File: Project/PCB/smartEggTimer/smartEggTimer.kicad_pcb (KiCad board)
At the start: 2 copper layers, 72 x 72 mm, 65 parts, among them J1 Conn_01x05_Pin, J2 Conn_01x03_Pin, J3 Conn_01x03_Pin, J4 Conn_01x06_Pin, J5 Conn_01x02_Socket, J6 Conn_01x02_Socket, J7 Conn_01x03_Pin, J8 Conn_01x03_Pin, Q2 STP60NF06L, SW1 SW_Push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

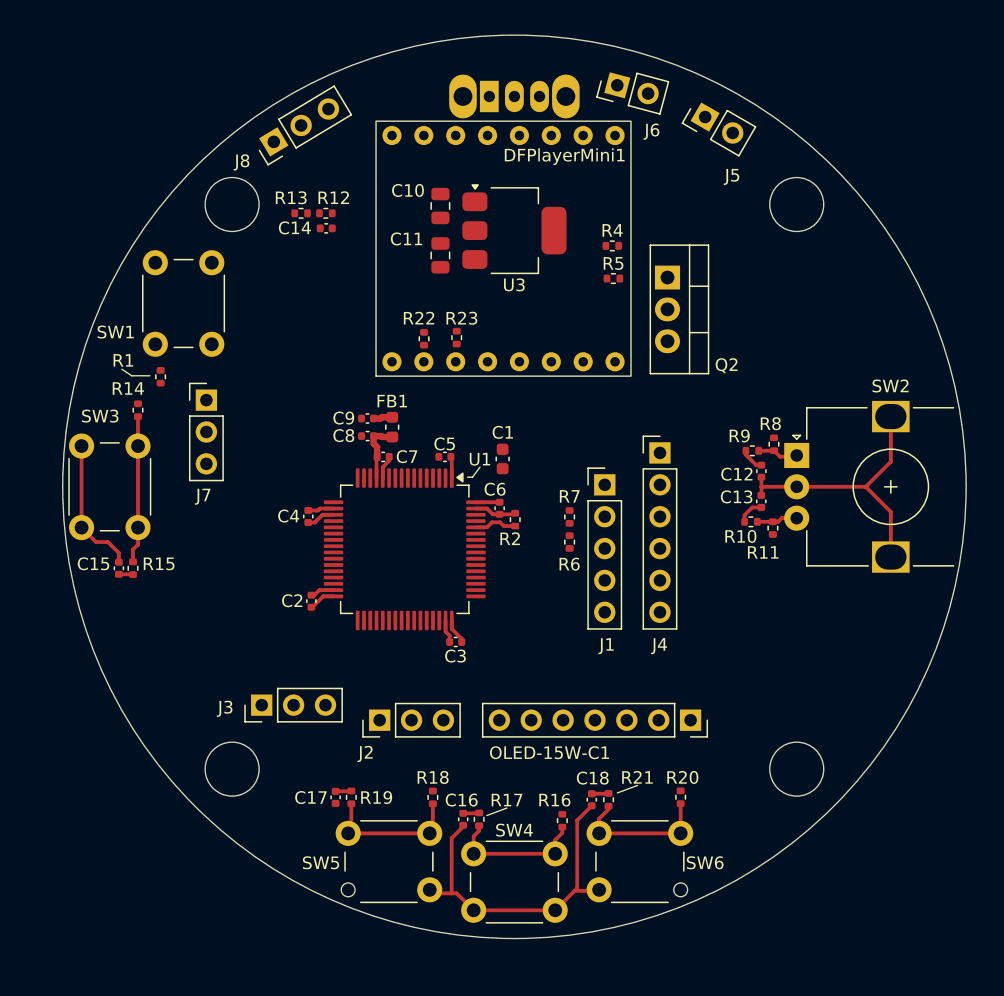
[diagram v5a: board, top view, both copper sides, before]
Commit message: finish PCB routing Further changes: - Change schematic symbol of MOSFET s.t. pin assignment is correct - Add STEP file for DFPlayer Mini - Save edited footprints to custom-parts project library - Set "exclude from BOM" attribute for components which will be soldered manually
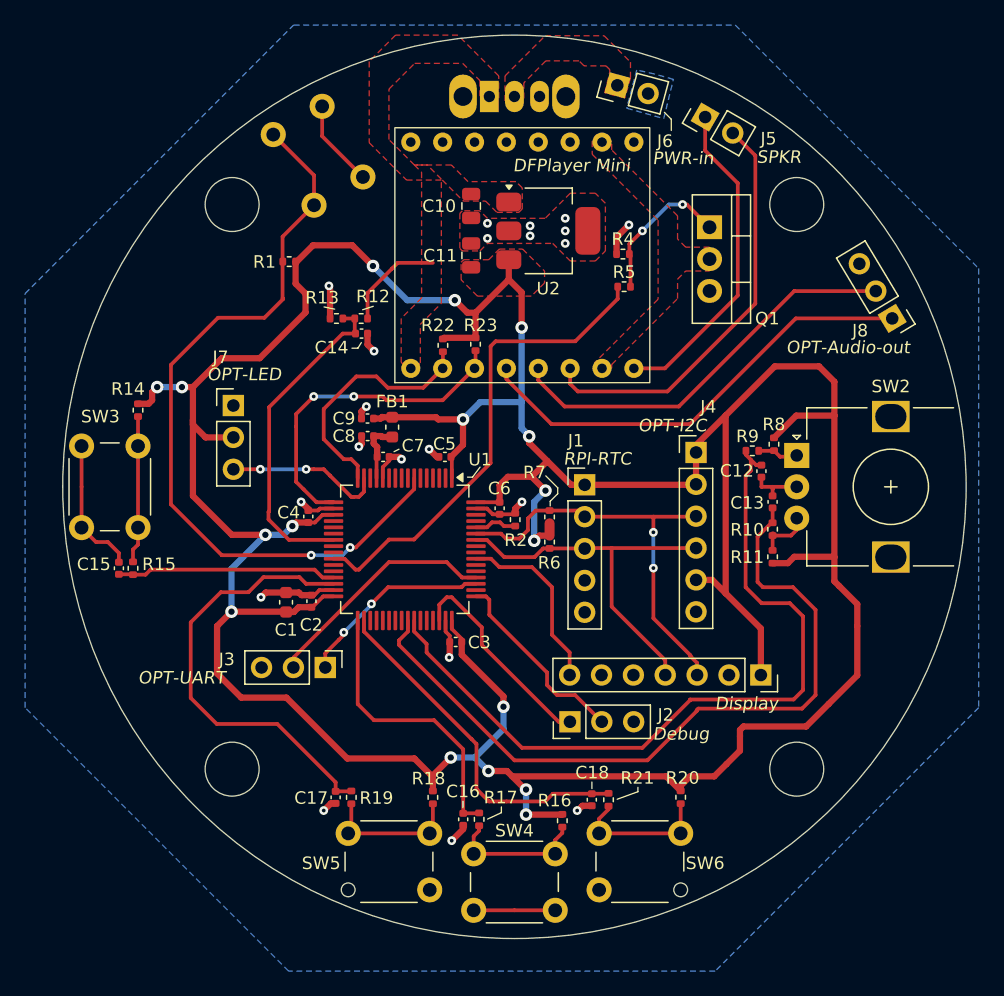
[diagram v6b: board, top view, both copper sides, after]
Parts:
- removed Q2: STP60NF06L, Package_TO_SOT_THT:TO-220-3_Vertical
- removed U3: AP7361C-33E, Package_TO_SOT_SMD:SOT-223-3_TabPin2
- added Q1: STP60NF06L, Package_TO_SOT_THT:TO-220-3_Vertical, F.Cu at (115.5, 79.3)
- added U2: AP7361C-33E, Package_TO_SOT_SMD:SOT-223-3_TabPin2, F.Cu at (102.7, 79.6)
- H1, H2: footprint MountingHole:MountingHole_4.3mm_M4 -> custom-parts:MountingHole_4.3mm_M4_Without-Screws
- H3, H8: footprint MountingHole:MountingHole_4.3mm_M4_DIN965 -> custom-parts:MountingHole_4.3mm_M4_Without-Screws
- SW1: moved to B.Cu
- SW2: footprint Rotary_Encoder:RotaryEncoder_Alps_EC12E_Vertical_H20mm -> custom-parts:RotaryEncoder_Alps_EC12E_Vertical_H20mm_Mounting-Holes-GND
- SW5: footprint Button_Switch_THT:SW_PUSH_6mm_H13mm -> custom-parts:SW_PUSH_6mm_H13mm_No-Pad_Top-Right
- SW6: footprint Button_Switch_THT:SW_PUSH_6mm_H13mm -> custom-parts:SW_PUSH_6mm_H13mm_No-Pad_Top-Left
- SW7: footprint Button_Switch_THT:SW_Slide_SPDT_Angled_CK_OS102011MA1Q -> custom-parts:SW_Slide_SPDT_Angled_CK_OS102011MA1Q_Protruding
- moved J8 51.3 mm to (130.1, 86.6), turned to -149 degrees
- moved SW1 21.3 mm to (87.9, 75.3), turned to 120 degrees
- moved C1 20.7 mm to (81.8, 109.2)
- moved J2 15.2 mm to (104.4, 118.7)
- moved R1 13.8 mm to (82.0, 82.0), turned to 0 degrees
- moved C14 8.84 mm to (87.8, 87.8)
- moved R12 8.84 mm to (87.8, 86.6)
- moved R13 8.84 mm to (85.8, 86.6)
- moved OLED-15W-C1 6.66 mm to (119.6, 115.0)
- moved J3 5.89 mm to (84.9, 114.4), turned to -90 degrees
- moved J4 2.88 mm to (114.5, 97.3)
- moved C10 2.45 mm to (96.5, 77.6)
- moved C11 2.45 mm to (96.5, 81.6)
- moved R11 2.29 mm to (120.6, 105.6)
- moved J7 2.19 mm to (77.6, 93.5)
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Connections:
- net Net-(Q2-D) renamed /DFPlayer-Minus
- J5 pad 1: /SPK+ -> /SPK-
- J5 pad 2: /SPK- -> /SPK+
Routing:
- net +3.3V: track 11.6 -> 316.9 mm, vias 0 -> 17
- net /NRST: track 0.00 -> 62.7 mm, vias 0 -> 2
- net /Rotary Encoder a: track 1.89 -> 61.7 mm
- net /Rotary Encoder b: track 2.12 -> 60.3 mm
- net /DFPlayer-On/Off switch: track 0.00 -> 38.4 mm
- net /DAC_R: track 0.00 -> 36.6 mm
- net /I2C1_SDA: track 0.00 -> 34.2 mm, vias 0 -> 2
- net /Button_2: track 1.26 -> 35.4 mm
- net /SPK+: track 0.00 -> 33.5 mm
- net /DAC_L: track 0.00 -> 32.5 mm
- net /I2C1_SCL: track 0.00 -> 30.3 mm
- net /USART2_RX: track 0.00 -> 28.0 mm, vias 0 -> 2
- net /Button_4: track 1.35 -> 28.3 mm
- net /Battery_indicator: track 0.00 -> 26.2 mm
- net /SPK-: track 0.00 -> 26.0 mm
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- added copper zone on F.Cu, net +3.3V
- added copper zone on F.Cu, net /Bat+
- added copper zone on F.Cu, net /Battery-SW
- added copper zone on F.Cu, net /DFPlayer-Minus
- added copper zone on B.Cu, net GND
- added copper zone on F.Cu, net GND
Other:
- board text added: "+"
- board text added: "-"
- board text added: "3V3"
- board text added: "A"
- board text added: "B"
- board text added: "D"
- board text added: "DAC_L"
- board text added: "DAC_R"
- board text added: "DFPlayer Mini"
- board text added: "Debug"
- board text added: "Display"
- board text added: "ESHO1 2024 Helge, Nico, Tobias 08/24 | V1.0"
- board text added: "G"
- board text added: "GND"
- board text added: "L"
- board text added: "LED-Data"
- board text added: "NC"
- board text added: "Note: Most of the Pin Headers / Sockets are just placeholders s.t. there will be enough space to hand-solder the external components to the PCB. They will not be included in the BOM."
- board text added: "OPT-Audio-out"
- board text added: "OPT-I2C"
- board text added: "OPT-LED"
- board text added: "OPT-UART"
- board text added: "PWR-in"
- board text added: "R"
- board text added: "RPI-RTC"
- board text added: "RST"
- board text added: "RX"
- board text added: "Reset"
- board text added: "S"
- board text added: "SCL"
- board text added: "SDA"
- board text added: "SPKR"
- board text added: "SPKR+"
- board text added: "SPKR-"
- board text added: "SWCLK"
- board text added: "SWD"
- board text added: "TX"
- board text added: "VCC"

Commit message: minor fixes on DFPlayer pin labels
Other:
- board text added: "to_nMOS"
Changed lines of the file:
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@@
 		(layer "Edge.Cuts")
+	)
+	(gr_text "to_nMOS"
+		(at 107.5 73.65 90)
+		(layer "B.SilkS")
+		(effects
+			(font
+				(size 1 1)
+				(thickness 0.153)
+			)
+			(justify left bottom mirror)
+		)
 	)
 	(gr_text "B"
@@
 		)
 	)
-	(gr_text "GND"
-		(at 107.55 86.3 90)
+	(gr_text "to_nMOS"
+		(at 107.525 83.25 90)
 		(layer "B.SilkS")
 		(effects
@@
 		)
 	)
-	(gr_text "RX"
+	(gr_text "TX"
 		(at 97.5 87.525 90)
 		(layer "B.SilkS")
@@
 	)
 	(gr_text "GND"
-		(at 107.6 73.675 90)
-		(layer "B.SilkS")
-		(effects
-			(font
-				(size 1 1)
-				(thickness 0.153)
-			)
-			(justify left bottom mirror)
-		)
-	)
-	(gr_text "GND"
 		(at 110.225 120.075 90)
 		(layer "B.SilkS")
@@
 		)
 	)
-	(gr_text "TX"
+	(gr_text "RX"
 		(at 94.9 87.55 90)
 		(layer "B.SilkS")

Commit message: generate files for manufacturing
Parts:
- FB1: value 120R -> 600R
